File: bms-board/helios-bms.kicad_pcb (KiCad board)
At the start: 2 copper layers, 0 parts

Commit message: fixed ERC errors
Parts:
- added C1: 10u, Capacitor_SMD:C_0603_1608Metric, F.Cu at (160.7, 67.8)
- added C10: 10u, Capacitor_SMD:C_0603_1608Metric, F.Cu at (160.7, 72.8)
- added C11: 470u, Capacitor_SMD:CP_Elec_10x10, F.Cu at (170.0, 72.4)
- added C12: 0.1u, Capacitor_SMD:C_0402_1005Metric, F.Cu at (181.1, 69.5)
- added C13: 2.2u, Capacitor_SMD:C_0402_1005Metric, F.Cu at (181.1, 71.4)
- added C14: 2.2u, Capacitor_SMD:C_0402_1005Metric, F.Cu at (181.1, 73.4)
- added C15: 0.1u, Capacitor_SMD:C_0402_1005Metric, F.Cu at (181.1, 75.4)
- added C16: 22p, Capacitor_SMD:C_0402_1005Metric, F.Cu at (181.1, 77.3)
- added C17: 10u, Capacitor_SMD:C_0603_1608Metric, F.Cu at (160.7, 75.3)
- added C18: 47n, Capacitor_SMD:C_0402_1005Metric, F.Cu at (184.0, 67.5)
- added C19: 22u, Capacitor_SMD:C_0603_1608Metric, F.Cu at (160.7, 77.8)
- added C2: 0.1u, Capacitor_SMD:C_0402_1005Metric, F.Cu at (178.2, 67.5)
- added C20: 470p, Capacitor_SMD:C_0402_1005Metric, F.Cu at (184.0, 69.5)
- added C21: 22u, Capacitor_SMD:C_0603_1608Metric, F.Cu at (160.7, 80.3)
- added C22: 10u, Capacitor_SMD:C_0603_1608Metric, F.Cu at (160.7, 82.8)
- added C23: 0.1u, Capacitor_SMD:C_0402_1005Metric, F.Cu at (184.0, 71.4)
- added C3: 1u, Capacitor_SMD:C_0402_1005Metric, F.Cu at (178.2, 69.5)
- added C4: 0.1u, Capacitor_SMD:C_0402_1005Metric, F.Cu at (178.2, 71.4)
- added C5: 1.5n, Capacitor_SMD:C_0402_1005Metric, F.Cu at (178.2, 73.4)
- added C6: 0.1u, Capacitor_SMD:C_0402_1005Metric, F.Cu at (178.2, 75.4)
- added C7: 22p, Capacitor_SMD:C_0402_1005Metric, F.Cu at (178.2, 77.3)
- added C8: 22u, Capacitor_SMD:C_0603_1608Metric, F.Cu at (160.7, 70.3)
- added C9: 1u, Capacitor_SMD:C_0402_1005Metric, F.Cu at (181.1, 67.5)
- added D1: Status, LED_SMD:LED_0402_1005Metric, F.Cu at (160.4, 85.1)
- added D2: TBD, Diode_SMD:D_0402_1005Metric, F.Cu at (160.4, 87.1)
- added J1: Debug, Connector:Tag-Connect_TC2030-IDC-NL_2x03_P1.27mm_Vertical, F.Cu at (189.4, 75.6)
- added J2: Output, Connector_JST:JST_ZE_SM03B-ZESS-TB_1x03-1MP_P1.50mm_Horizontal, F.Cu at (180.4, 95.0)
- added J3: Umbilical, Connector_JST:JST_ZE_SM04B-ZESS-TB_1x04-1MP_P1.50mm_Horizontal, F.Cu at (181.1, 83.4)
- added L1: 3.3uH, Inductor_SMD:L_Taiyo-Yuden_NR-50xx, F.Cu at (166.0, 95.6)
- added L2: 2.2uH, Inductor_SMD:L_0805_2012Metric, F.Cu at (171.6, 98.2)
- added Q1: NMOS, Helios-BMS:SOT-1220_UDFN6B_TOS-L, F.Cu at (190.2, 80.1)
- added Q2: SSM3J332R, Helios-BMS:SOT-1220_UDFN6B_TOS-L, F.Cu at (190.2, 83.6)
- added R1: TBD, Resistor_SMD:R_0402_1005Metric, F.Cu at (164.2, 79.3)
- added R10: 150k, Resistor_SMD:R_0402_1005Metric, F.Cu at (167.1, 83.3)
- added R11: 49.9k, Resistor_SMD:R_0402_1005Metric, F.Cu at (167.1, 85.3)
- added R12: 10k, Resistor_SMD:R_0402_1005Metric, F.Cu at (167.1, 87.3)
- added R13: 160k, Resistor_SMD:R_0402_1005Metric, F.Cu at (167.1, 89.3)
- added R14: 300, Resistor_SMD:R_0402_1005Metric, F.Cu at (167.1, 91.3)
- added R15: 36k, Resistor_SMD:R_0402_1005Metric, F.Cu at (170.0, 79.3)
- added R16: 10k, Resistor_SMD:R_0402_1005Metric, F.Cu at (170.0, 81.3)
- added R17: 10k, Resistor_SMD:R_0402_1005Metric, F.Cu at (170.0, 83.3)
- added R18: 10k, Resistor_SMD:R_0402_1005Metric, F.Cu at (170.0, 85.3)
- added R19: 1.1M, Resistor_SMD:R_0402_1005Metric, F.Cu at (170.0, 87.3)
- added R2: 62k, Resistor_SMD:R_0402_1005Metric, F.Cu at (164.2, 81.3)
- added R20: 200k, Resistor_SMD:R_0402_1005Metric, F.Cu at (170.0, 89.3)
- added R21: 100k, Resistor_SMD:R_0402_1005Metric, F.Cu at (170.0, 91.3)
- added R22: 10k, Resistor_SMD:R_0402_1005Metric, F.Cu at (172.9, 79.3)
- added R23: 10k, Resistor_SMD:R_0402_1005Metric, F.Cu at (172.9, 81.3)
- added R24: 120, Resistor_SMD:R_0402_1005Metric, F.Cu at (172.9, 83.3)
- added R3: 30k, Resistor_SMD:R_0402_1005Metric, F.Cu at (164.2, 83.3)
- added R4: 430k, Resistor_SMD:R_0402_1005Metric, F.Cu at (164.2, 85.3)
- added R5: 100k, Resistor_SMD:R_0402_1005Metric, F.Cu at (164.2, 87.3)
- added R6: 51k, Resistor_SMD:R_0402_1005Metric, F.Cu at (164.2, 89.3)
- added R7: 137k, Resistor_SMD:R_0402_1005Metric, F.Cu at (164.2, 91.3)
- added R8: 30k, Resistor_SMD:R_0402_1005Metric, F.Cu at (167.1, 79.3)
- added R9: 1k, Resistor_SMD:R_0402_1005Metric, F.Cu at (167.1, 81.3)
- added U1: TPSM86125x, Helios-BMS:Texas-QFN-FCMOD-7_4x3.3mm, F.Cu at (189.6, 92.9)
- added U2: STM32L011F4Ux, Package_DFN_QFN:ST_UFQFPN-20_3x3mm_P0.5mm, F.Cu at (171.8, 94.6)
- added U3: TPS22811, Helios-BMS:TPS22811, F.Cu at (190.3, 87.3)
- added U4: TPS563207s, Package_TO_SOT_SMD:SOT-563, F.Cu at (160.4, 89.7)
- added U5: BQ25306, Package_DFN_QFN:WQFN-16-1EP_3x3mm_P0.5mm_EP1.68x1.68mm_ThermalVias, F.Cu at (189.4, 98.3)
- added U6: THVD1400D, Package_SO:SOIC-8_3.9x4.9mm_P1.27mm, F.Cu at (189.6, 69.9)

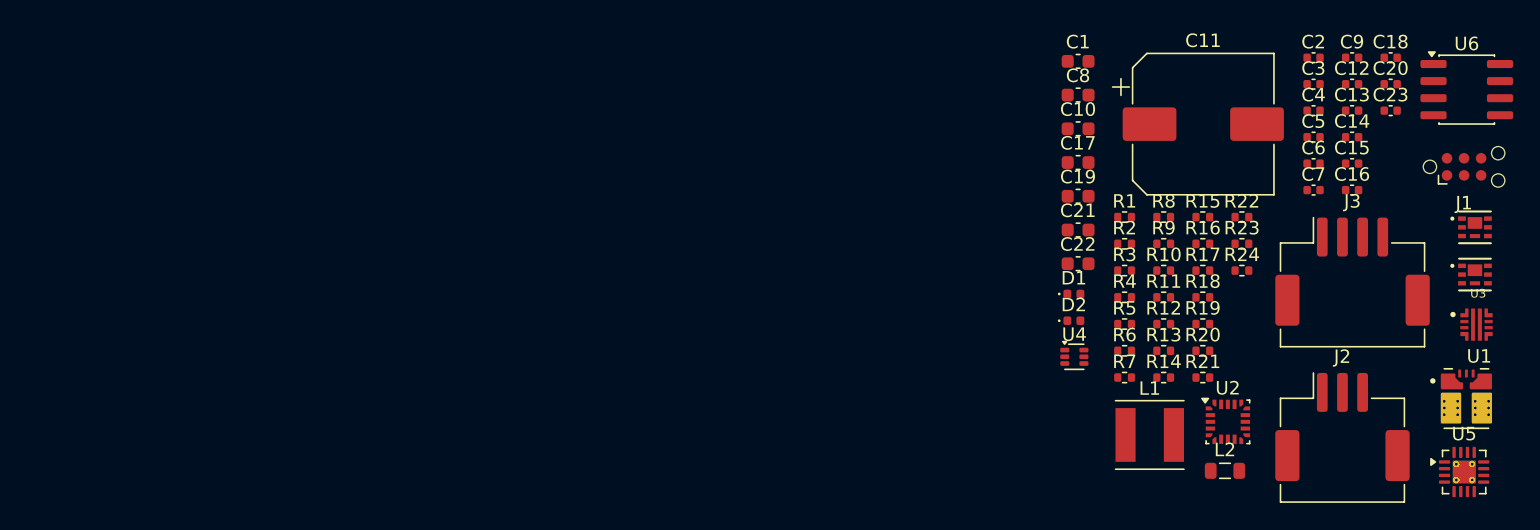
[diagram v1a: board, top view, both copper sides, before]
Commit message: routed 2layer 2oz, gonna change to 4layer 1oz
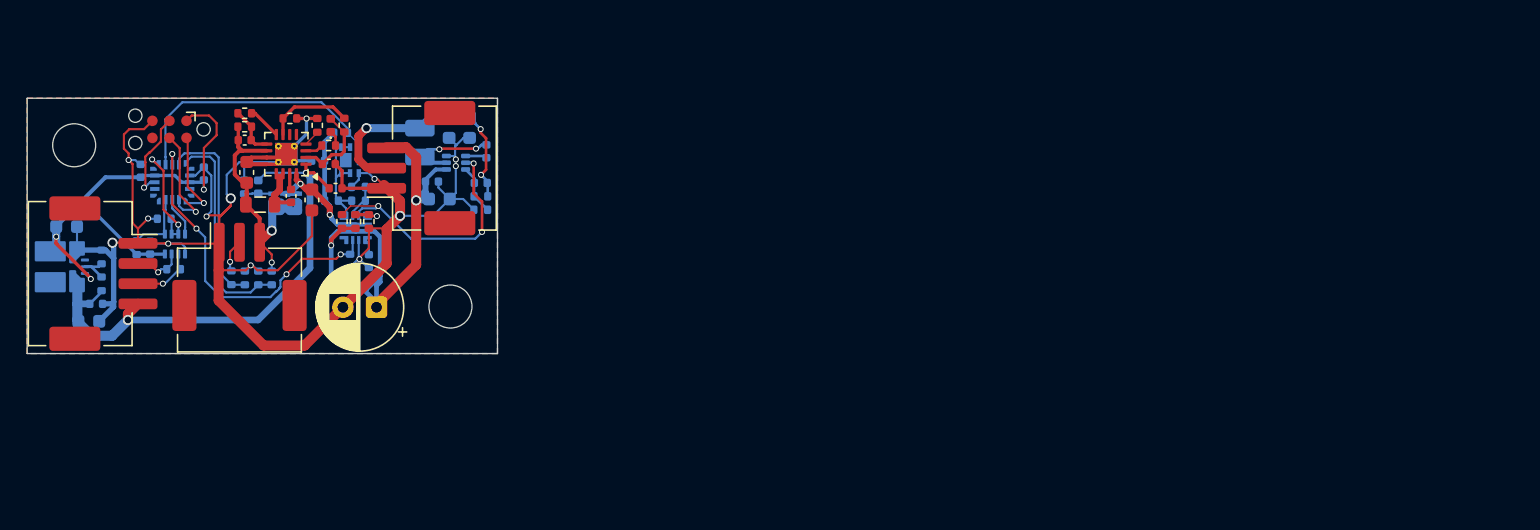
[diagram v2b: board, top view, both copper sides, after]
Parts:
- removed C7: 22p, Capacitor_SMD:C_0402_1005Metric
- added H1: MountingHole, MountingHole:MountingHole_3.2mm_M3_DIN965, F.Cu at (114.0, 86.0)
- added H2: MountingHole, MountingHole:MountingHole_3.2mm_M3_DIN965, F.Cu at (86.0, 74.0)
- added J4: Battery, Connector_JST:JST_ZE_SM03B-ZESS-TB_1x03-1MP_P1.50mm_Horizontal, F.Cu at (98.3, 83.8)
- added R25: 100k, Resistor_SMD:R_0402_1005Metric, B.Cu at (97.7, 83.9)
- added R26: 300k, Resistor_SMD:R_0402_1005Metric, B.Cu at (98.7, 83.9)
- C1, C10, C12, C15, C16, C19, C2, C21, C23, C3, C4, C5, C6, C8, C9, D2, Q1, Q2, R1, R15, R16, R2, R21, R22, R23, R24, R3, R4, R5, R6, R9, U2, U3, U4: moved to B.Cu
- C11: footprint Capacitor_SMD:CP_Elec_10x10 -> Capacitor_THT:CP_Radial_D6.3mm_P2.50mm
- J3: value Umbilical -> Outboard
- L1: footprint Inductor_SMD:L_Taiyo-Yuden_NR-50xx -> Inductor_SMD:L_1008_2520Metric; moved to B.Cu
- R7: value 137k -> 500k; moved to B.Cu
- R8: value 30k -> 300k; moved to B.Cu
- U1: value TPSM86125x -> TPSM861253; moved to B.Cu
- U6: footprint Package_SO:SOIC-8_3.9x4.9mm_P1.27mm -> Package_TO_SOT_SMD:SOT-583-8; moved to B.Cu
- moved U1 105.2 mm to (84.9, 83.0), turned to 90 degrees
- moved U6 96.8 mm to (93.5, 81.3), turned to -90 degrees
- moved J1 96.4 mm to (93.1, 72.8), turned to 180 degrees
- moved J3 93.0 mm to (88.2, 83.5), turned to -90 degrees
- moved C23 92.9 mm to (91.7, 81.6), turned to 90 degrees
- moved C2 92.4 mm to (87.6, 85.8)
- moved U5 90.8 mm to (101.8, 74.7), turned to 180 degrees
- moved Q2 88.7 mm to (101.7, 78.2)
- moved C6 87.3 mm to (91.0, 75.9), turned to 90 degrees
- moved C20 85.4 mm to (98.7, 73.6)
- moved Q1 83.9 mm to (106.5, 75.1), turned to -90 degrees
- moved U3 83.7 mm to (107.0, 80.2), turned to -90 degrees
- moved C4 82.7 mm to (95.7, 76.1), turned to 90 degrees
- moved C18 82.5 mm to (102.1, 77.8), turned to 90 degrees
- moved R22 82.3 mm to (90.7, 81.6), turned to 90 degrees
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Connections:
- R7 pad 1: +3.3V -> +BATT
- R7 pad 2: Net-(U1-VOS) -> /PACK_ADC
- R8 pad 1: Net-(U1-VOS) -> /PACK_ADC
- U1 pad 7: Net-(U1-VOS) -> +3.3V
- U2 pad 10: unconnected-(U2-PA7-Pad10) -> /PACK_ADC
- U2 pad 7: unconnected-(U2-PA4-Pad7) -> /GATE
- U2 pad 8: /GATE -> /IMON
- U2 pad 9: /IMON -> /CENTER_TAP_ADC
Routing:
- net GND: track 0.00 -> 141.9 mm, vias 0 -> 13
- net +VSW: track 0.00 -> 41.4 mm, vias 0 -> 2
- net +12V: track 0.00 -> 40.2 mm, vias 0 -> 2
- net +3.3V: track 0.00 -> 37.0 mm, vias 0 -> 3
- net /IMON: track 0.00 -> 25.3 mm, vias 0 -> 4
- net +BATT: track 0.00 -> 21.9 mm, vias 0 -> 2
- net /GATE: track 0.00 -> 20.0 mm
- net /SW_PG: track 0.00 -> 19.8 mm, vias 0 -> 3
- net +3V7: track 0.00 -> 19.7 mm, vias 0 -> 3
- net /PACK_ADC: track 0.00 -> 16.2 mm
- net VSYS: track 0.00 -> 15.6 mm, vias 0 -> 2
- net /CENTER_TAP_ADC: track 0.00 -> 14.6 mm
- net /EN/UVLO: track 0.00 -> 8.63 mm
- net /DE: track 0.00 -> 8.62 mm, vias 0 -> 2
- net /SWCLK: track 0.00 -> 8.20 mm, vias 0 -> 1
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- added copper zone on B.Cu, net GND
- added copper zone on F.Cu, net GND
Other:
- board outline added: 35 x 19 mm
- copper layers 2 -> 4

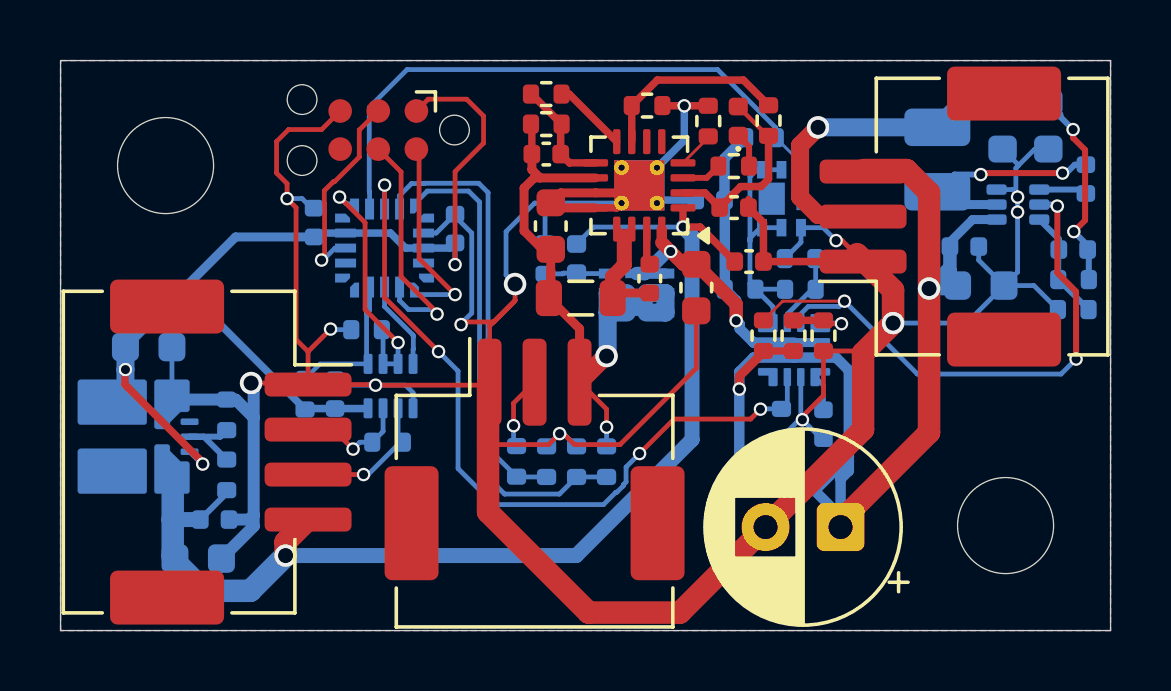
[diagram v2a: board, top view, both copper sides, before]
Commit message: rerouted for 4 layers
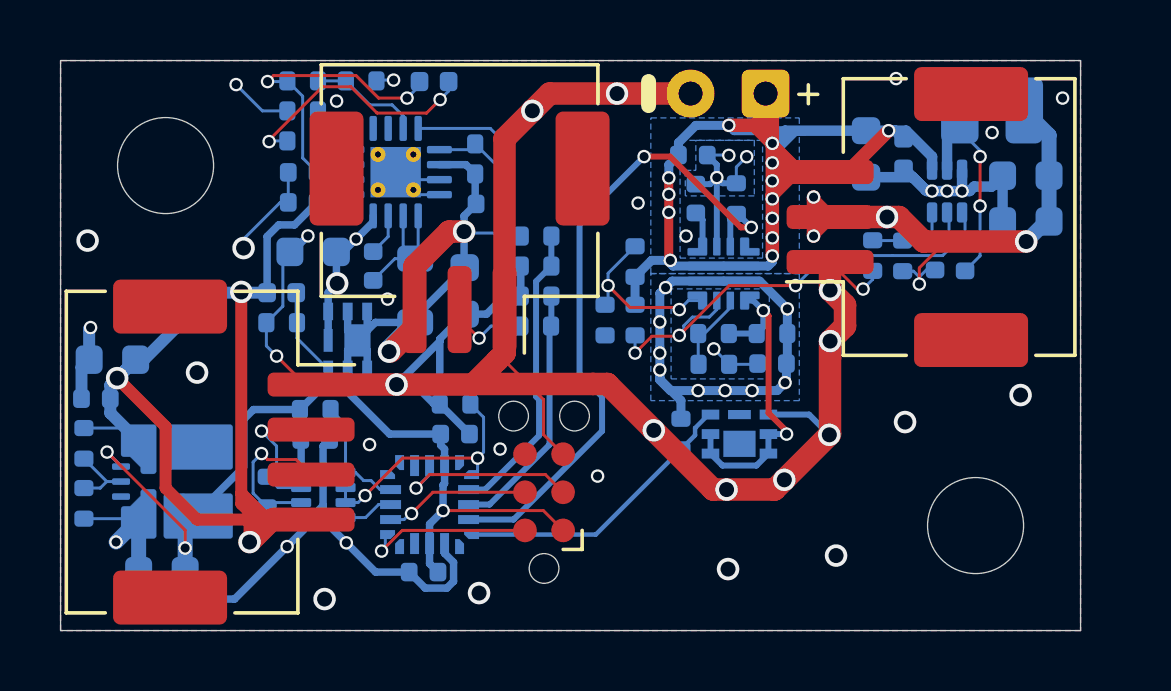
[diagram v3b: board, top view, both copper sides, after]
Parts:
- C13, C14, C17, C18, C20, C22, D1, L2, R10, R11, R12, R13, R14, R17, R18, R19, R20, U5: moved to B.Cu
- moved R17 15.6 mm to (90.6, 71.2), turned to 180 degrees
- moved C13 15.0 mm to (90.6, 75.2), turned to 180 degrees
- moved C11 14.7 mm to (106.0, 71.6)
- moved C14 14.4 mm to (90.6, 74.2), turned to 180 degrees
- moved R14 14.4 mm to (90.6, 73.2), turned to 0 degrees
- moved R13 13.5 mm to (90.6, 72.2), turned to 180 degrees
- moved J1 13.3 mm to (98.6, 84.9), turned to 90 degrees
- moved C17 12.8 mm to (90.9, 76.9), turned to 180 degrees
- moved C4 11.5 mm to (94.6, 87.5), turned to 180 degrees
- moved C9 10.8 mm to (103.6, 73.7)
- moved R1 10.2 mm to (103.2, 83.0), turned to -90 degrees
- moved D1 10.2 mm to (95.0, 71.2), turned to 180 degrees
- moved D2 9.90 mm to (89.9, 78.2), turned to 180 degrees
- moved Q2 9.76 mm to (92.1, 79.8), turned to 90 degrees
- moved R18 9.57 mm to (92.5, 71.2)
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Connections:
- U2 pad 10: /PACK_ADC -> /GATE
- U2 pad 7: /GATE -> /PACK_ADC
- U2 pad 8: /IMON -> /CENTER_TAP_ADC
- U2 pad 9: /CENTER_TAP_ADC -> /IMON
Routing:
- net GND: track 141.9 -> 118.1 mm, vias 13 -> 44
- net +VSW: track 41.4 -> 56.3 mm, vias 2 -> 13
- net /GATE: track 20.0 -> 9.69 mm
- net Net-(D1-K): track 1.16 -> 8.38 mm, vias 0 -> 2
- net /PACK_ADC: track 16.2 -> 10.00 mm
- net /CENTER_TAP_ADC: track 14.6 -> 8.50 mm
- net VSYS: track 15.6 -> 21.7 mm, vias 2 -> 11
- net +3.3V: track 37.0 -> 31.1 mm
- net /REGN: track 6.30 -> 10.9 mm, vias 0 -> 2
- net /SW_PG: track 19.8 -> 15.9 mm
- net Net-(U3-PGTH): track 2.53 -> 6.09 mm, vias 1 -> 2
- net /SWCLK: track 8.20 -> 4.86 mm
- net /IMON: track 25.3 -> 22.4 mm, vias 4 -> 2
- net Net-(U5-TS): track 6.46 -> 3.74 mm
- net /EN/UVLO: track 8.63 -> 11.2 mm, vias 0 -> 2
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- added copper zone on In2.Cu, net +12V
- added copper zone on In2.Cu, net +3V7
- added copper zone on B.Cu, net +VSW
- added copper zone on In2.Cu, net +VSW
- added copper zone on In1.Cu, net GND
- added copper zone on B.Cu, net VSYS
- added copper zone on In2.Cu, net VSYS
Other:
- board size 35 x 19 mm -> 34 x 19 mm
